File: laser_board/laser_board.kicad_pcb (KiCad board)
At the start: 2 copper layers, 35 parts, among them IC1 ATMEGA328P-P, Q1 IRF540N, SW1 SW_PUSH, U1 LM317T, Y1 Crystal

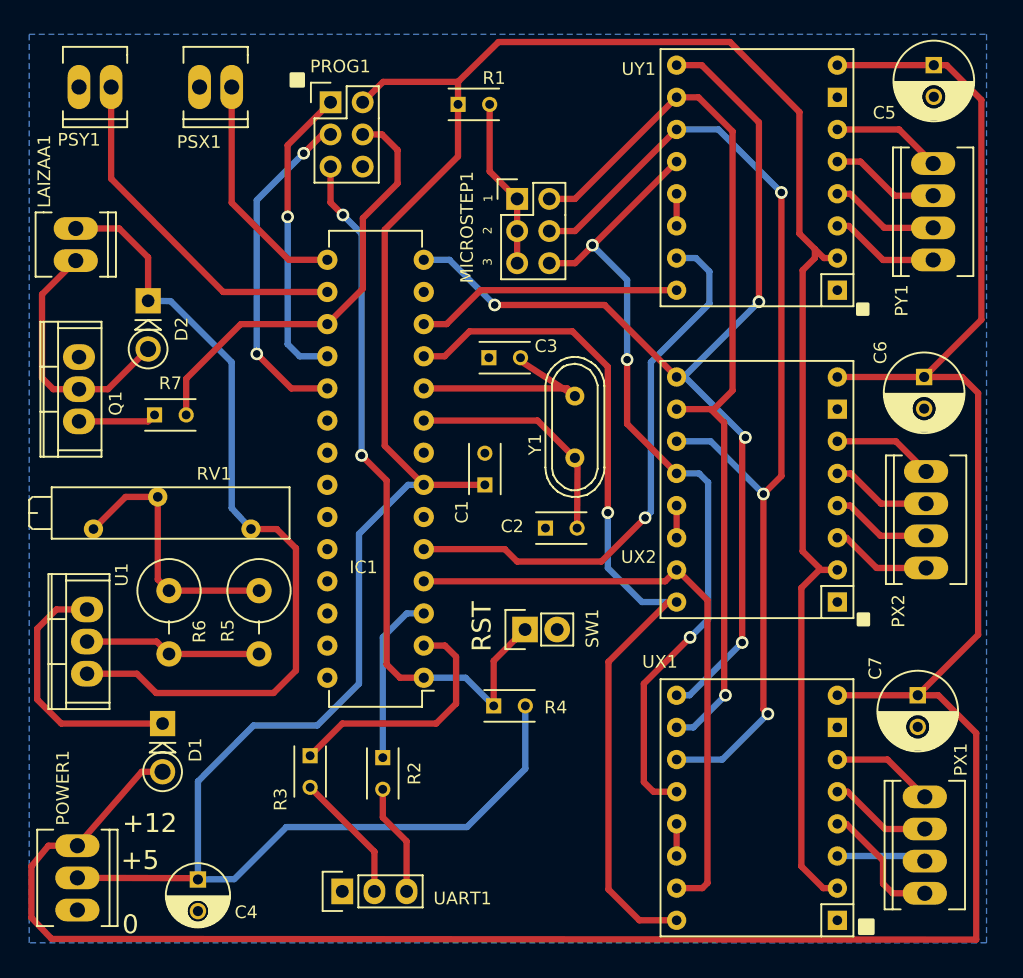
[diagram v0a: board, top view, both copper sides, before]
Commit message: Fixing the board margins
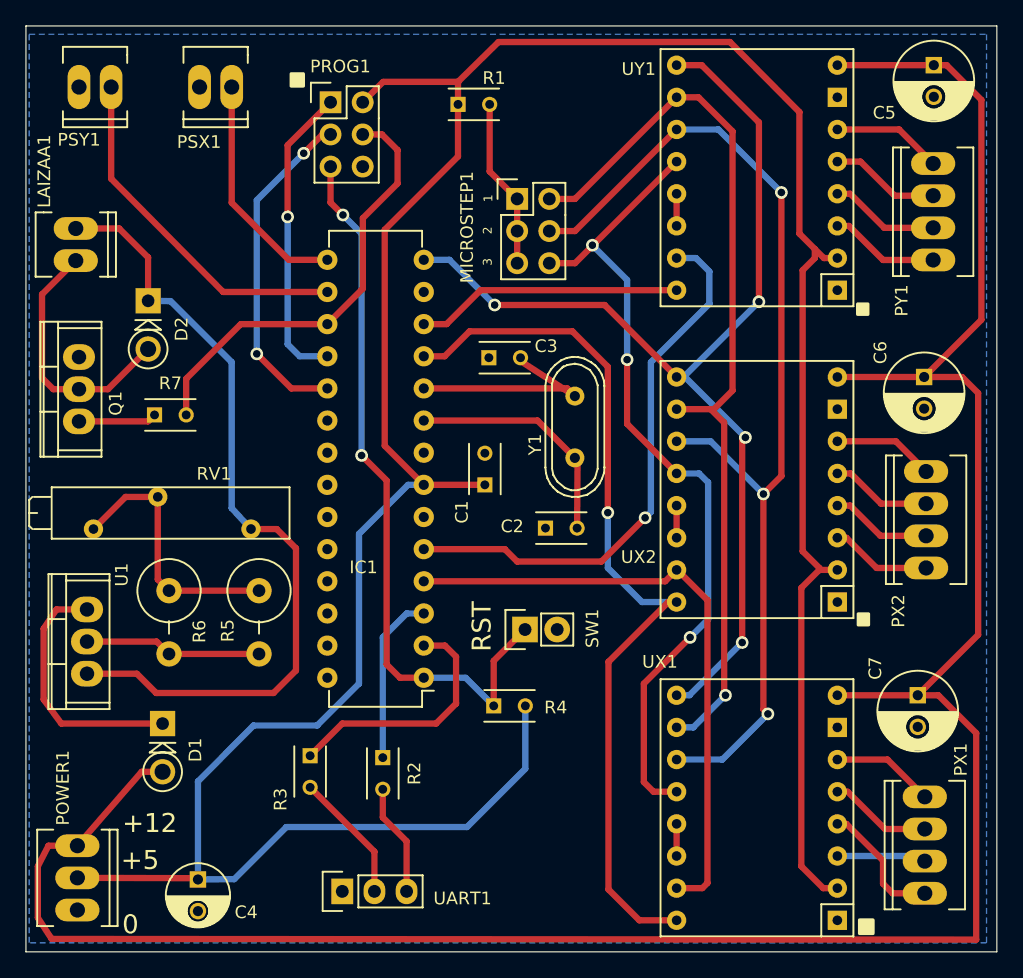
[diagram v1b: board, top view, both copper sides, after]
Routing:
- net Net-(D1-Pad1): track 20.9 -> 20.2 mm
- net +12V: track 195.5 -> 194.9 mm
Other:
- board outline added: 76.7 x 73.2 mm
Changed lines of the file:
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@@
     (links 102)
     (no_connects 0)
-    (area 122.835999 36.475999 200.252001 110.844001)
+    (area 123.322999 37.033999 200.202001 110.286001)
     (thickness 1.6)
-    (drawings 12)
+    (drawings 11)
     (tracks 311)
     (zones 0)
@@
     (visible_elements FFFFFF7F)
     (pcbplotparams
-      (layerselection 0x00030_80000001)
+      (layerselection 0x010fc_80000001)
       (usegerberextensions false)
       (excludeedgelayer true)
@@
       (outputformat 1)
       (mirror false)
-      (drillshape 1)
+      (drillshape 0)
       (scaleselection 1)
       (outputdirectory ""))
@@
       (net 8 "Net-(D2-Pad1)"))
   )
-  (gr_line (start 200.152 36.576) (end 200.152 37.084) (angle 90) (layer Margin) (width 0.2))
-  (gr_line (start 122.936 36.576) (end 200.152 36.576) (angle 90) (layer Margin) (width 0.2))
-  (gr_line (start 122.936 110.744) (end 122.936 36.576) (angle 90) (layer Margin) (width 0.2))
-  (gr_line (start 200.152 110.744) (end 122.936 110.744) (angle 90) (layer Margin) (width 0.2))
-  (gr_line (start 200.152 37.084) (end 200.152 110.744) (angle 90) (layer Margin) (width 0.2))
+  (gr_line (start 123.444 37.084) (end 200.152 37.084) (angle 90) (layer Edge.Cuts) (width 0.1))
+  (gr_line (start 123.444 110.236) (end 123.444 37.084) (angle 90) (layer Edge.Cuts) (width 0.1))
+  (gr_line (start 200.152 110.236) (end 123.444 110.236) (angle 90) (layer Edge.Cuts) (width 0.1))
+  (gr_line (start 200.152 37.084) (end 200.152 110.236) (angle 90) (layer Edge.Cuts) (width 0.1))
   (gr_text RST (at 159.4612 84.5312 90) (layer F.SilkS)
     (effects (font (size 1.5 1.5) (thickness 0.3)))
@@
   (segment (start 198.5264 92.964) (end 198.5264 109.2708) (width 0.5) (layer F.Cu) (net 5))
   (segment (start 198.5264 109.2708) (end 125.476 109.22) (width 0.5) (layer F.Cu) (net 5))
-  (segment (start 125.476 109.22) (end 123.8758 107.5436) (width 0.5) (layer F.Cu) (net 5))
-  (segment (start 123.8758 107.5436) (end 123.8758 103.4796) (width 0.5) (layer F.Cu) (net 5))
-  (segment (start 123.8758 103.4796) (end 125.222 101.854) (width 0.5) (layer F.Cu) (net 5))
+  (segment (start 125.476 109.22) (end 124.3838 107.5436) (width 0.5) (layer F.Cu) (net 5))
+  (segment (start 124.3838 107.5436) (end 124.3838 103.4796) (width 0.5) (layer F.Cu) (net 5))
+  (segment (start 124.3838 103.4796) (end 125.222 101.854) (width 0.5) (layer F.Cu) (net 5))
   (segment (start 125.222 101.854) (end 127.508 101.854) (width 0.5) (layer F.Cu) (net 5) (status 20))
   (segment (start 187.5536 89.9668) (end 193.9036 89.9668) (width 0.5) (layer F.Cu) (net 5))
@@
   (segment (start 128.27 83.185) (end 125.857 83.185) (width 0.5) (layer F.Cu) (net 6))
   (segment (start 126.238 92.202) (end 134.239 92.202) (width 0.5) (layer F.Cu) (net 6))
-  (segment (start 124.333 90.297) (end 126.238 92.202) (width 0.5) (layer F.Cu) (net 6))
-  (segment (start 124.333 84.709) (end 124.333 90.297) (width 0.5) (layer F.Cu) (net 6))
-  (segment (start 125.857 83.185) (end 124.333 84.709) (width 0.5) (layer F.Cu) (net 6))
+  (segment (start 124.841 90.297) (end 126.238 92.202) (width 0.5) (layer F.Cu) (net 6))
+  (segment (start 124.841 84.709) (end 124.841 90.297) (width 0.5) (layer F.Cu) (net 6))
+  (segment (start 125.857 83.185) (end 124.841 84.709) (width 0.5) (layer F.Cu) (net 6))
   (segment (start 127.635 65.786) (end 129.921 65.786) (width 0.5) (layer F.Cu) (net 7))
   (segment (start 129.921 65.786) (end 133.096 62.611) (width 0.5) (layer F.Cu) (net 7))

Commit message: major PCB improvements
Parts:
- SW1: footprint Pin_Headers:Pin_Header_Straight_1x02 -> laser_footprints:SIMPLE_SWITCH
- moved SW1 0.90 mm to (163.6, 85.3), turned to 0 degrees
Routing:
- net Net-(IC1-Pad1): track 58.0 -> 56.5 mm
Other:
- board text added: "+"
- board text added: "-"
- board text added: "GND"
- board text added: "RX"
- board text added: "TX"

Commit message: laisaa board v01
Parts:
- added REF**: MountingHole_3.2mm_M3, Mounting_Holes:MountingHole_3.2mm_M3, F.Cu at (195.8, 41.0)
- added REF**: MountingHole_3.2mm_M3, Mounting_Holes:MountingHole_3.2mm_M3, F.Cu at (135.8, 104.3)
- added REF**: MountingHole_3.2mm_M3, Mounting_Holes:MountingHole_3.2mm_M3, F.Cu at (194.1, 105.2)
- added REF**: MountingHole_3.2mm_M3, Mounting_Holes:MountingHole_3.2mm_M3, F.Cu at (127.5, 42.2)
- moved C4 8.35 mm to (138.3, 96.3)
- moved C5 6.45 mm to (193.3, 46.4)
- moved POWER1 6.37 mm to (128.0, 98.0)
- moved PX1 5.79 mm to (194.6, 96.0)
- moved PSY1 5.36 mm to (134.1, 43.2)
- moved C7 5.17 mm to (194.6, 84.8)
- moved PY1 5.05 mm to (194.4, 56.8)
- moved PSX1 2.62 mm to (140.7, 43.2)
- turned D1 to 0 degrees
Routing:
- net +5V: track 234.1 -> 223.6 mm
- net +12V: track 194.9 -> 201.6 mm
- net Net-(IC1-Pad16): track 28.1 -> 22.4 mm
- net Net-(PY1-Pad1): track 8.68 -> 12.7 mm
- net Net-(PY1-Pad4): track 8.68 -> 12.3 mm
- net Net-(PY1-Pad2): track 8.68 -> 12.2 mm
- net Net-(PX1-Pad1): track 10.3 -> 7.14 mm
- net Net-(PY1-Pad3): track 8.68 -> 11.6 mm
- net Net-(PX1-Pad2): track 7.08 -> 9.36 mm
- net Net-(IC1-Pad15): track 18.6 -> 16.8 mm
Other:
- board text added: "C3E5"
- board text added: "Laizaa v01"
- board text added: "github.com/c3e5"

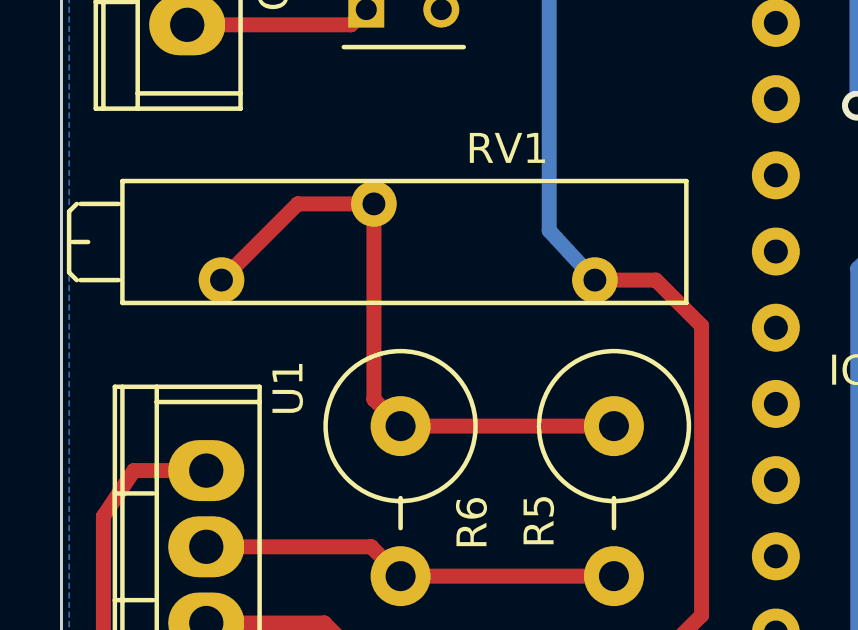
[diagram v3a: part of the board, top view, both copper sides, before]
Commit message: fix a pot route in the laser board
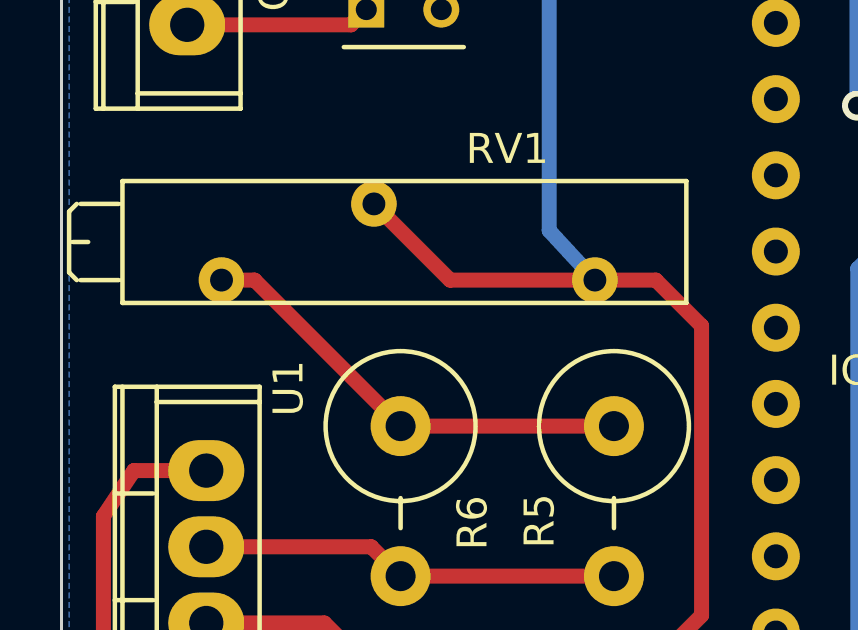
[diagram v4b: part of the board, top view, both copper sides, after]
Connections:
- RV1 pad 2: Net-(R5-Pad1) -> Net-(D2-Pad1)
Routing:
- net Net-(D2-Pad1): track 64.2 -> 72.6 mm
- net Net-(R5-Pad1): track 21.0 -> 15.1 mm
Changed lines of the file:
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@@
       (net 51 "Net-(R5-Pad1)"))
     (pad 2 thru_hole circle (at -7.366 -2.54) (size 1.524 1.524) (drill 0.762) (layers *.Cu *.Mask F.SilkS)
-      (net 51 "Net-(R5-Pad1)"))
+      (net 8 "Net-(D2-Pad1)"))
     (pad 1 thru_hole circle (at 0 0) (size 1.524 1.524) (drill 0.762) (layers *.Cu *.Mask F.SilkS)
       (net 8 "Net-(D2-Pad1)"))
@@
   (segment (start 129.921 65.786) (end 133.096 62.611) (width 0.5) (layer F.Cu) (net 7))
   (segment (start 127.635 65.786) (end 129.921 65.786) (width 0.5) (layer F.Cu) (net 7))
+  (segment (start 133.858 74.295) (end 136.398 76.835) (width 0.5) (layer F.Cu) (net 8))
+  (segment (start 136.398 76.835) (end 141.224 76.835) (width 0.5) (layer F.Cu) (net 8))
   (segment (start 134.874 58.8264) (end 139.7 63.6524) (width 0.5) (layer B.Cu) (net 8))
   (segment (start 139.7 63.6524) (end 139.7 75.184) (width 0.5) (layer B.Cu) (net 8))
@@
   (segment (start 150.9776 102.322) (end 145.8976 97.242) (width 0.5) (layer F.Cu) (net 50))
   (segment (start 150.9776 105.4608) (end 150.9776 102.322) (width 0.5) (layer F.Cu) (net 50))
-  (segment (start 131.318 74.295) (end 133.858 74.295) (width 0.5) (layer F.Cu) (net 51) (status 20))
-  (segment (start 128.778 76.835) (end 131.318 74.295) (width 0.5) (layer F.Cu) (net 51) (status 10))
+  (segment (start 128.778 76.835) (end 129.88036 76.835) (width 0.5) (layer F.Cu) (net 51))
+  (segment (start 129.88036 76.835) (end 134.747 81.70164) (width 0.5) (layer F.Cu) (net 51))
   (segment (start 134.747 81.70164) (end 141.859 81.70164) (width 0.5) (layer F.Cu) (net 51))
-  (segment (start 133.858 80.81264) (end 134.747 81.70164) (width 0.5) (layer F.Cu) (net 51))
-  (segment (start 133.858 74.295) (end 133.858 80.81264) (width 0.5) (layer F.Cu) (net 51))
   (segment (start 141.859 86.7029) (end 134.747 86.7029) (width 0.5) (layer F.Cu) (net 52))
   (segment (start 133.7691 85.725) (end 134.747 86.7029) (width 0.5) (layer F.Cu) (net 52))
